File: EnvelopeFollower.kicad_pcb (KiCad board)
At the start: 2 copper layers, 177.9 x 87.9 mm, 87 parts, among them J1 RTip, J10 IN, J11 GND, J12 GND, J13 SW1B, J14 OUT, J15 DTIP, J16 DSW, J17 GND, J18 ITIP, J19 ISLV, J20 SW1C, J3 +9v, J4 GND, J5 SEND, J6 RSLV, J7 GND, J8 GND, J9 SW1A, SW1 Moog, SW2 BANDWIDTH, SW3 MODE, U1 TL074, U2 LM1458, U3 VTL5C, U4 VTL5C

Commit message: V2.00 provisionaly completed
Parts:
- removed U3, U4: VTL5C, OptoDevice:PerkinElmer_VTL5C
- added J2: 1A3, Connector_Wire:SolderWire-0.25sqmm_1x01_D0.65mm_OD1.7mm, F.Cu at (125.7, 117.4)
- added J21: 1B2, Connector_Wire:SolderWire-0.25sqmm_1x01_D0.65mm_OD1.7mm, F.Cu at (132.2, 117.4)
- added J22: 1B1, Connector_Wire:SolderWire-0.25sqmm_1x01_D0.65mm_OD1.7mm, F.Cu at (128.9, 117.4)
- added J23: 1C1, Connector_Wire:SolderWire-0.25sqmm_1x01_D0.65mm_OD1.7mm, F.Cu at (138.7, 117.5)
- added J24: 1C2, Connector_Wire:SolderWire-0.25sqmm_1x01_D0.65mm_OD1.7mm, F.Cu at (142.0, 117.5)
- added J25: 1C3, Connector_Wire:SolderWire-0.25sqmm_1x01_D0.65mm_OD1.7mm, F.Cu at (145.2, 117.5)
- added V1D1: D_Photo, MyLibrary:LED_D5.0mm, F.Cu at (121.6, 79.9)
- added V1R1: D_LDR, MyLibrary:R_LDR_5.2x5.2mm_P3.5mm_Horizontal, F.Cu at (106.8, 79.2)
- added V2D1: D_Photo, MyLibrary:LED_D5.0mm, F.Cu at (110.8, 143.4)
- added V2R1: D_LDR, MyLibrary:R_LDR_5.2x5.2mm_P3.5mm_Horizontal, F.Cu at (96.5, 143.1)
- C2: footprint Capacitor_THT:CP_Radial_D5.0mm_P2.00mm -> MyLibrary:CP_Radial_D5.0mm_PWideForPower
- J13: value SW1B -> 1A1; footprint Connector_Wire:SolderWire-0.25sqmm_1x03_P4.2mm_D0.65mm_OD1.7mm -> Connector_Wire:SolderWire-0.25sqmm_1x01_D0.65mm_OD1.7mm
- J20: value SW1C -> 1B3; footprint Connector_Wire:SolderWire-0.25sqmm_1x03_P4.2mm_D0.65mm_OD1.7mm -> Connector_Wire:SolderWire-0.25sqmm_1x01_D0.65mm_OD1.7mm
- J9: value SW1A -> 1A2; footprint Connector_Wire:SolderWire-0.25sqmm_1x03_P4.2mm_D0.65mm_OD1.7mm -> Connector_Wire:SolderWire-0.25sqmm_1x01_D0.65mm_OD1.7mm
- R22: value 1M8 -> 330r
- SW1: footprint Switches:SWITCH_SPDT_PTH_11.6X4.0MM -> MyLibrary:SWITCH_SPDT_PTH_12.9X6.9MM
- moved C3 149.5 mm to (70.5, 76.1), turned to 0 degrees
- moved C2 142.6 mm to (72.0, 70.6), turned to 0 degrees
- moved D1 141.0 mm to (72.3, 57.6), turned to 90 degrees
- moved R5 139.8 mm to (74.0, 81.2), turned to 0 degrees
- moved R6 118.4 mm to (81.4, 78.0)
- moved C5 118.0 mm to (87.8, 74.5), turned to 90 degrees
- moved C14 89.8 mm to (96.4, 69.9)
- moved C15 80.3 mm to (107.1, 133.2), turned to 90 degrees
- moved R11 54.2 mm to (114.1, 111.5), turned to 0 degrees
- moved G*** 43.6 mm to (182.9, 80.7)
- moved D2 40.7 mm to (103.3, 121.6), turned to 0 degrees
- moved R14 40.6 mm to (99.7, 76.8), turned to 180 degrees
- moved G*** 39.1 mm to (178.0, 77.5)
- moved R13 38.4 mm to (99.8, 80.9)
- moved C16 37.7 mm to (143.2, 110.3), turned to 180 degrees
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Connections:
- net /Vact1-4 renamed Net-(C6-Pad2)
- J13 pad 1: Net-(J13-Pad1) -> Net-(J10-Pad1)
- J14 pad 1: Net-(J13-Pad2) -> Net-(J14-Pad1)
- J20 pad 1: Net-(D7-Pad1) -> Net-(J10-Pad1)
- J9 pad 1: Net-(J10-Pad1) -> Net-(C15-Pad1)
- R14 pad 1: Net-(J13-Pad1) -> Net-(J22-Pad1)
- R19 pad 2: /Vact1-2 -> Net-(R19-Pad2)
- R20 pad 2: /Vact2-2 -> Net-(R20-Pad2)
- RV1 pad 1: /Mode2 -> Net-(R1-Pad1)
- RV1 pad 3: Net-(R1-Pad1) -> /Mode2
- RV2 pad 1: GND -> Net-(C14-Pad2)
- RV2 pad 3: Net-(C14-Pad2) -> GND
- RV3 pad 1: Net-(C14-Pad1) -> /ModeA
- RV3 pad 3: /ModeA -> Net-(C14-Pad1)
- RV4 pad 1: Net-(R17-Pad2) -> Net-(C20-Pad1)
- RV4 pad 3: Net-(C20-Pad1) -> Net-(R17-Pad2)
- RV5 pad 1: Net-(R18-Pad2) -> Net-(J15-Pad1)
- RV5 pad 3: Net-(J15-Pad1) -> Net-(R18-Pad2)
- RV6 pad 1: Net-(J18-Pad1) -> /UDB
- RV6 pad 3: /UDB -> Net-(J18-Pad1)
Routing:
- net Net-(J13-Pad2): track 218.1 -> 0.00 mm
- net Net-(J13-Pad1): track 189.6 -> 0.00 mm, vias 1 -> 0
- net Net-(C14-Pad1): track 396.1 -> 209.0 mm, vias 4 -> 0
- net +9VA: track 155.0 -> 7.19 mm
- net Net-(J14-Pad1): track 0.00 -> 122.5 mm
- net VCC: track 219.3 -> 115.6 mm, vias 0 -> 2
- net Net-(R20-Pad2): track 0.00 -> 103.2 mm
- net /Vact2-2: track 102.6 -> 0.00 mm
- net /Vact1-2: track 96.1 -> 0.00 mm, vias 1 -> 0
- net Net-(J10-Pad1): track 127.5 -> 220.9 mm
- net /UD6: track 174.0 -> 266.5 mm, vias 2 -> 0
- net Net-(C17-Pad2): track 9.73 -> 75.4 mm
- net GND: track 0.00 -> 63.2 mm, vias 5 -> 2
- net Net-(J22-Pad1): track 0.00 -> 58.2 mm
- net Net-(C15-Pad1): track 71.1 -> 26.3 mm
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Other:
- board size 177.9 x 87.9 mm -> 138 x 114 mm
- net class Power added: clearance 0.5, trace_width 0.5, via_dia 0.8, via_drill 0.4
- net class VCC added: clearance 0.35, trace_width 0.35, via_dia 0.8, via_drill 0.4
- board text added: "A1"
- board text added: "A2"
- board text added: "A3"
- board text added: "ATTACK"
- board text added: "B1"
- board text added: "B2"
- board text added: "B3"
- board text added: "BLEND"
- board text added: "BYPASS"
- board text added: "C1"
- board text added: "C2"
- board text added: "C3"
- board text added: "COLOUR"
- board text added: "DC IN"
- board text added: "DECAY"
- board text added: "INTENSITY"
- board text added: "SENSITIVITY"
- board text added: "V2.0"
- board text removed: "1A"
- board text removed: "2A"
- board text removed: "3A"
- board text removed: "ATTACK B5K"
- board text removed: "BANDWIDTH"
- board text removed: "BLEND B10K"
- board text removed: "COLOUR B100K"
- board text removed: "DECAY A100K"
- board text removed: "INTENSITY B1K"
- board text removed: "MODE"
- board text removed: "POWER"
- board text removed: "RANGE"
- board text removed: "SENSITIVITY B10K"
- board text removed: "UP/DOWN"
- board text removed: "V1.0"

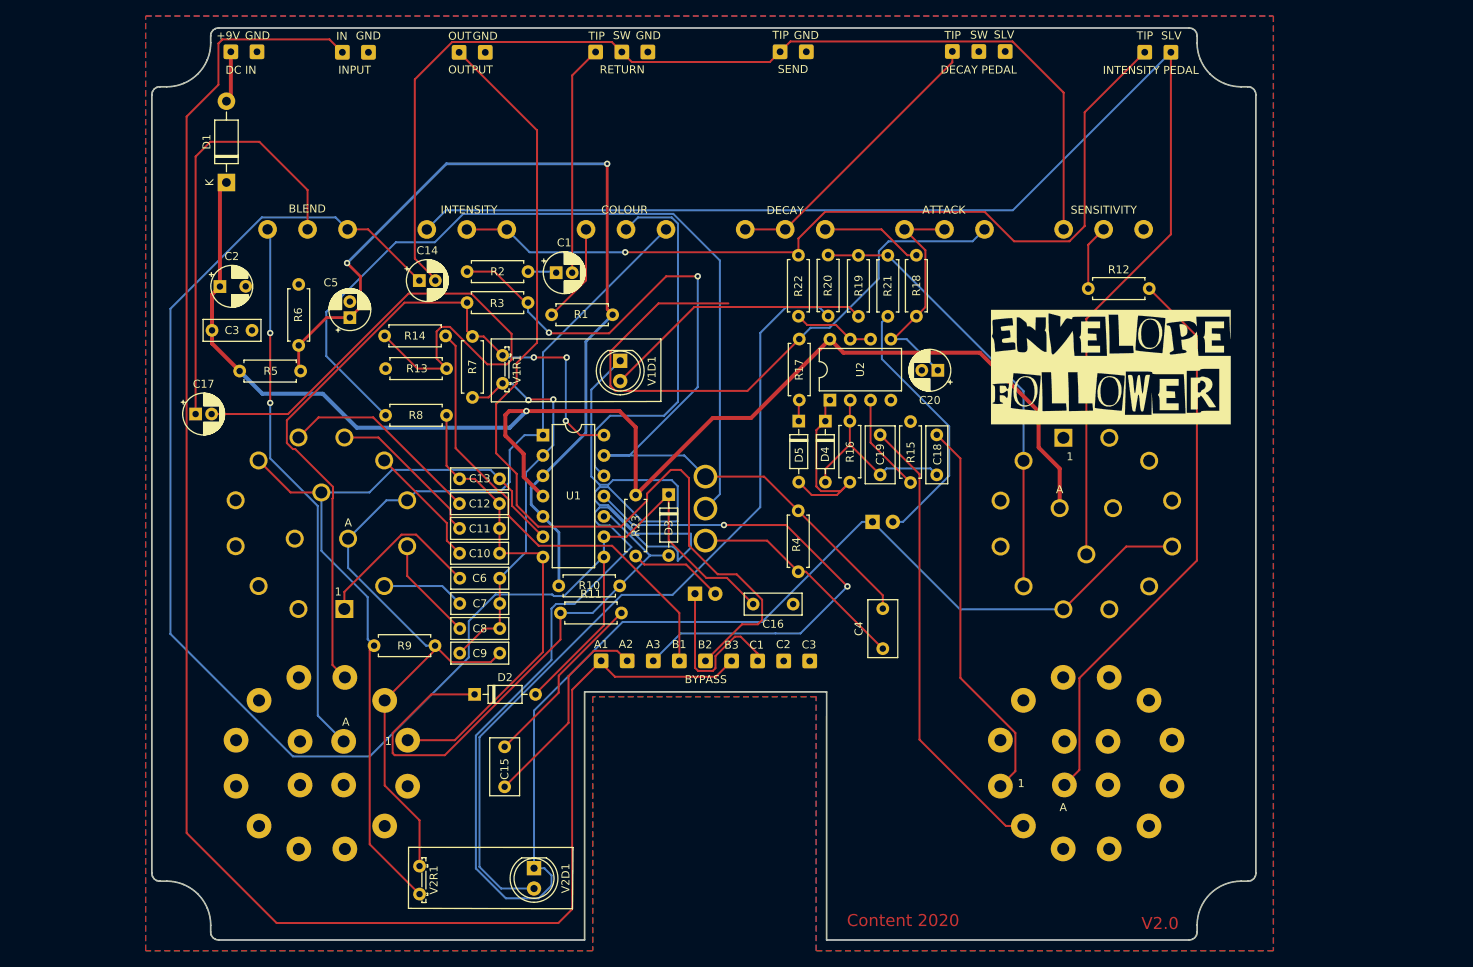
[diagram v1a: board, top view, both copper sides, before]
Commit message: cleaned up silks
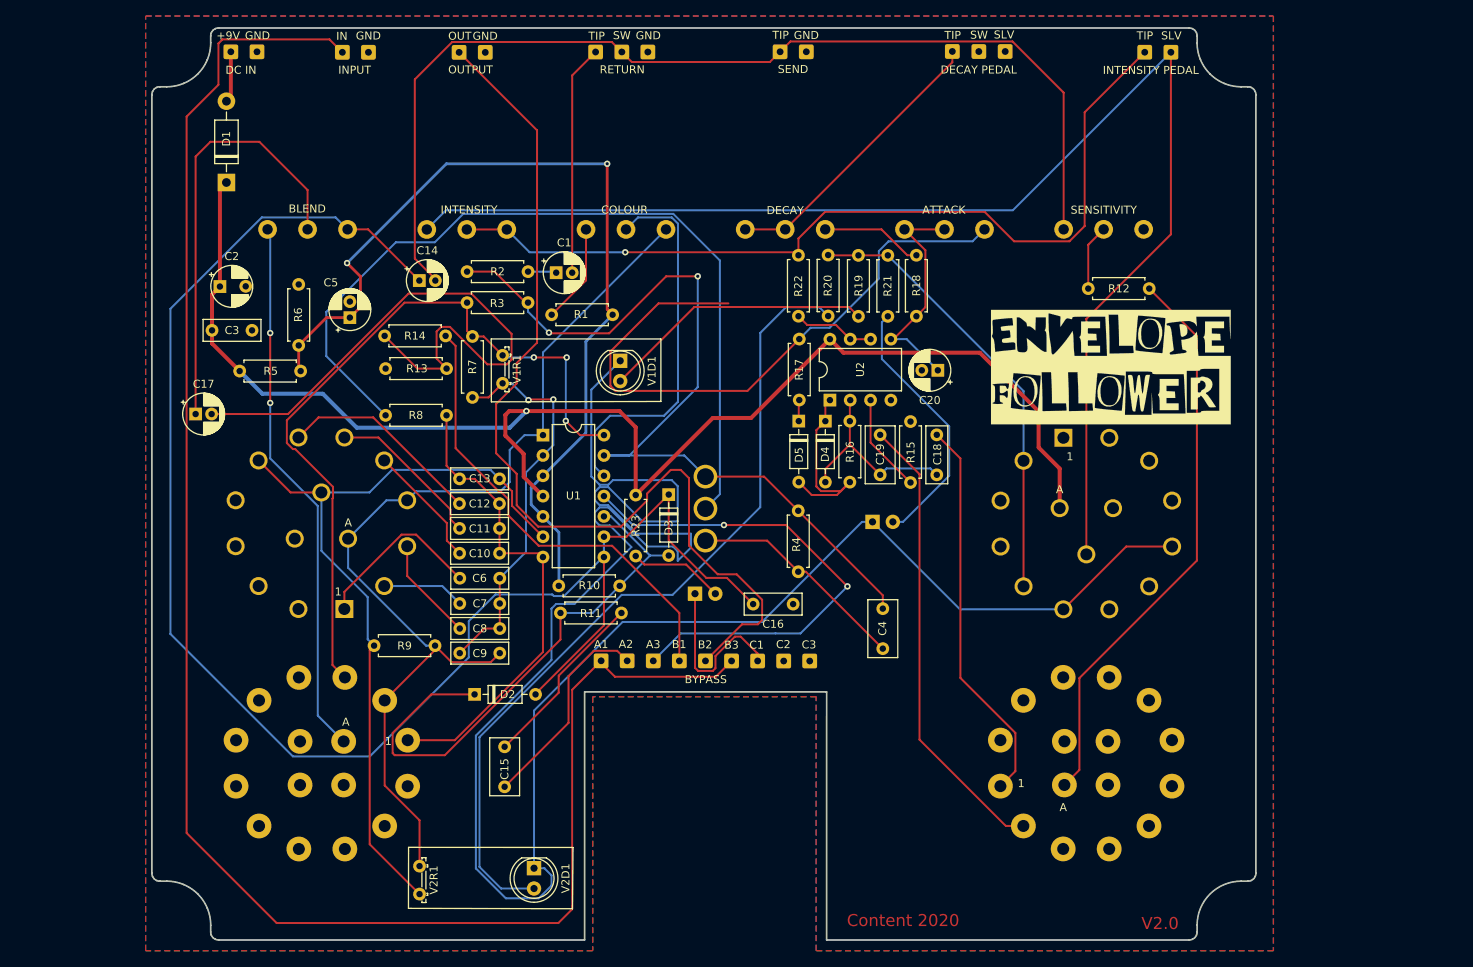
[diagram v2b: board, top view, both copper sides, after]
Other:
- rule pad_to_mask_clearance: 0.051 -> 0
